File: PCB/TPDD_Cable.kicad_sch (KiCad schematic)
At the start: 9 parts, among them J1 TPDD_RS-232C, P3 RX, P4 RTS, P5 CTS, P6 DSR, Q1 DTA114EKA, Q2 DTA114EKA, Q3 DTA114EKA

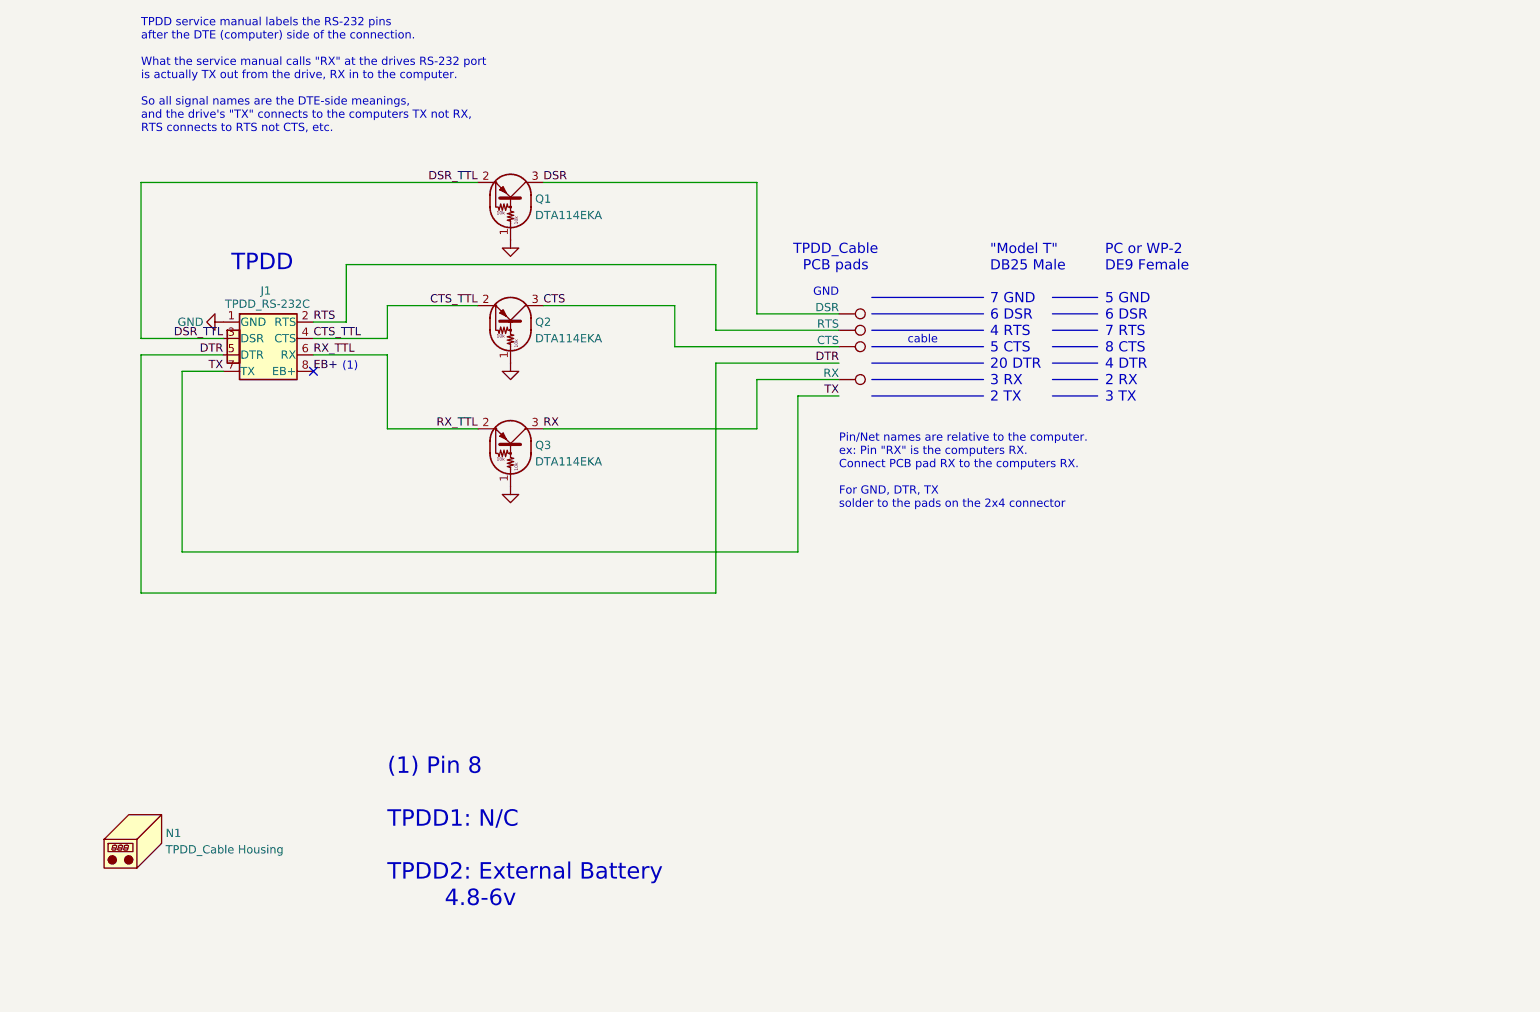
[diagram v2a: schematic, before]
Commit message: db25 pinout pics, enlarge ziptie holes to 3mm
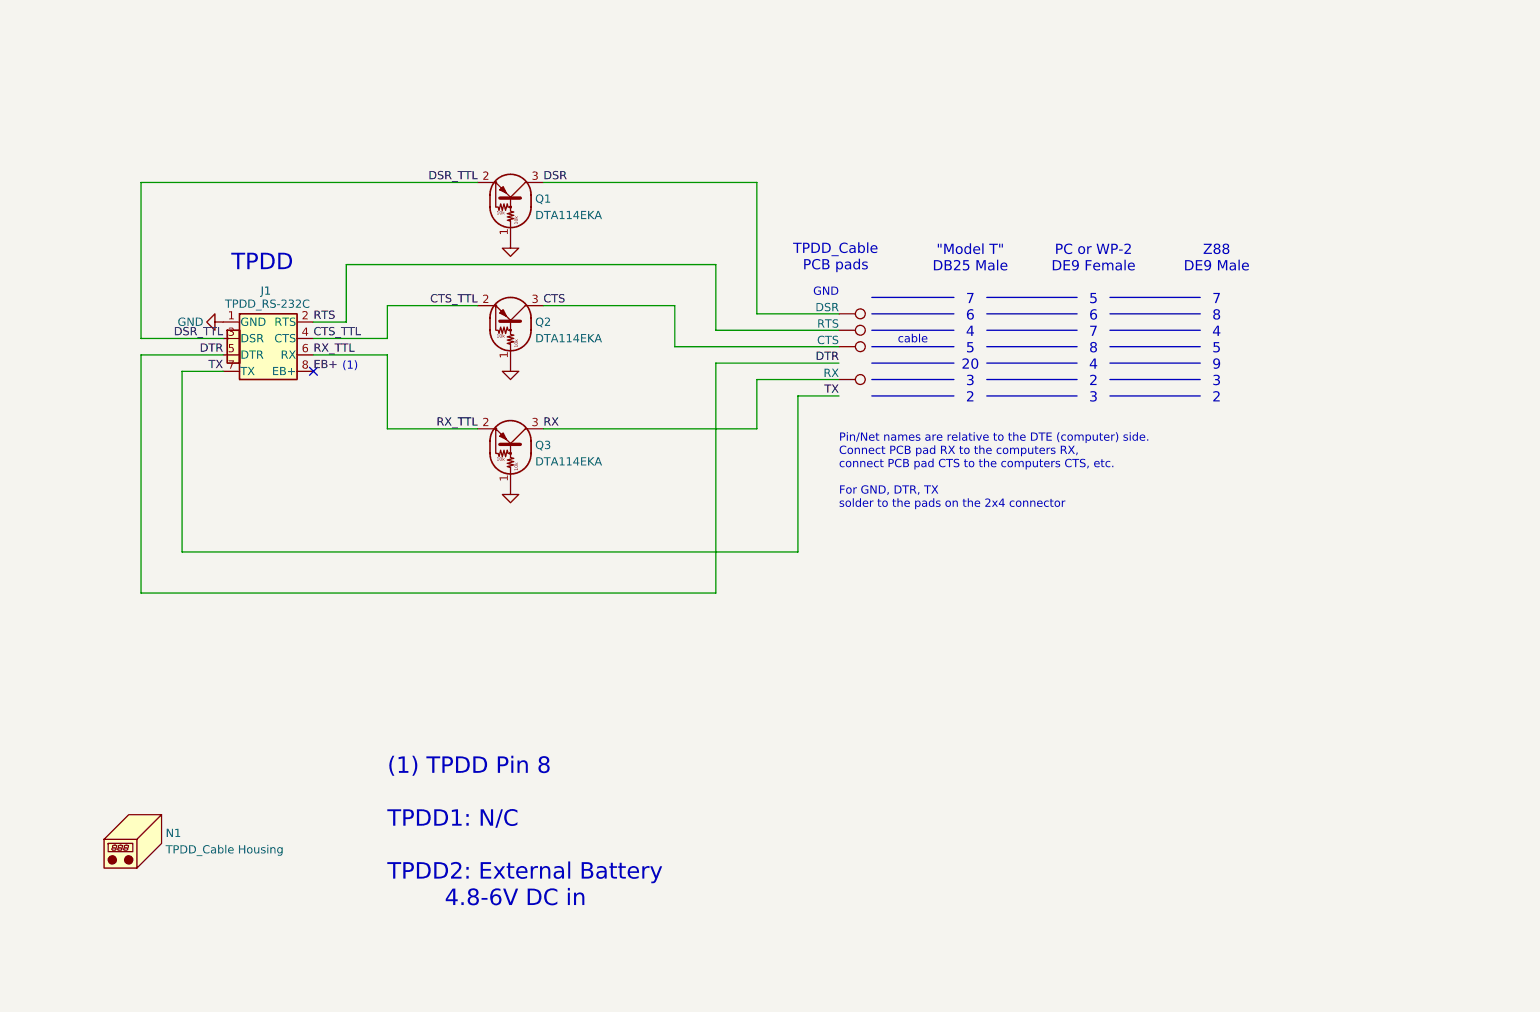
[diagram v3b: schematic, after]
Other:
- note added: ""Model T" DB25 Male 7 6 4 5 20 3 2"
- note added: "(1) TPDD Pin 8 TPDD1: N/C TPDD2: External Battery 4.8-6V DC in"
- note added: "PC or WP-2 DE9 Female 5 6 7 8 4 2 3"
- note added: "Pin/Net names are relative to the DTE (computer) side. Connect PCB pad RX to the computers RX, connect PCB pad CTS to the computers CTS, etc. For GND, DTR, TX solder to the pads on the 2x4 connector"
- note added: "Z88 DE9 Male 7 8 4 5 9 3 2"
- note removed: ""Model T" DB25 Male 7 GND 6 DSR 4 RTS 5 CTS 20 DTR 3 RX 2 TX"
- note removed: "(1) Pin 8 TPDD1: N/C TPDD2: External Battery 4.8-6v"
- note removed: "PC or WP-2 DE9 Female 5 GND 6 DSR 7 RTS 8 CTS 4 DTR 2 RX 3 TX"
- note removed: "Pin/Net names are relative to the computer. ex: Pin "RX" is the computers RX. Connect PCB pad RX to the computers RX. For GND, DTR, TX solder to the pads on the 2x4 connector"
- note removed: "TPDD service manual labels the RS-232 pins after the DTE (computer) side of the connection. What the service manual calls "RX" at the drives RS-232 port is actually TX out from the drive, RX in to the computer. So all signal names are the DTE-side meanings, and the drive's "TX" connects to the computers TX not RX, RTS connects to RTS not CTS, etc."
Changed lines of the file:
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@@
 		(title "TPDD-RS-232")
 		(date "2024-10-23")
-		(rev "5")
+		(rev "6")
 		(company "Brian K. White")
 	)
@@
 	(polyline
 		(pts
-			(xy 204.47 96.52) (xy 211.455 96.52)
+			(xy 194.31 96.52) (xy 208.28 96.52)
 		)
 		(stroke
@@
 	(polyline
 		(pts
-			(xy 204.47 86.36) (xy 211.455 86.36)
-		)
-		(stroke
-			(width 0)
-			(type default)
-		)
-	)
-	(polyline
-		(pts
-			(xy 176.53 86.36) (xy 193.802 86.36)
+			(xy 194.31 86.36) (xy 208.28 86.36)
+		)
+		(stroke
+			(width 0)
+			(type default)
+		)
+	)
+	(polyline
+		(pts
+			(xy 213.36 88.9) (xy 227.33 88.9)
+		)
+		(stroke
+			(width 0)
+			(type default)
+		)
+	)
+	(polyline
+		(pts
+			(xy 176.53 86.36) (xy 189.23 86.36)
+		)
+		(stroke
+			(width 0)
+			(type default)
+		)
+	)
+	(polyline
+		(pts
+			(xy 213.36 96.52) (xy 227.33 96.52)
 		)
 		(stroke
@@
 	(polyline
 		(pts
-			(xy 176.53 93.98) (xy 193.802 93.98)
+			(xy 176.53 93.98) (xy 189.23 93.98)
 		)
 		(stroke
@@
 	(polyline
 		(pts
-			(xy 204.47 81.28) (xy 211.455 81.28)
+			(xy 194.31 81.28) (xy 208.28 81.28)
 		)
 		(stroke
@@
 	(polyline
 		(pts
-			(xy 176.53 88.9) (xy 193.802 88.9)
+			(xy 176.53 88.9) (xy 189.23 88.9)
 		)
 		(stroke
@@
 		)
 	)
+	(polyline
+		(pts
+			(xy 213.36 86.36) (xy 227.33 86.36)
+		)
+		(stroke
+			(width 0)
+			(type default)
+		)
+	)
 	(wire
 		(pts
@@
 		)
 	)
+	(polyline
+		(pts
+			(xy 213.36 91.44) (xy 227.33 91.44)
+		)
+		(stroke
+			(width 0)
+			(type default)
+		)
+	)
 	(wire
 		(pts
@@
 	(polyline
 		(pts
-			(xy 204.47 88.9) (xy 211.455 88.9)
-		)
-		(stroke
-			(width 0)
-			(type default)
-		)
-	)
-	(polyline
-		(pts
-			(xy 176.53 81.28) (xy 193.802 81.28)
+			(xy 194.31 88.9) (xy 208.28 88.9)
+		)
+		(stroke
+			(width 0)
+			(type default)
+		)
+	)
+	(polyline
+		(pts
+			(xy 213.36 83.82) (xy 227.33 83.82)
+		)
+		(stroke
+			(width 0)
+			(type default)
+		)
+	)
+	(polyline
+		(pts
+			(xy 176.53 81.28) (xy 189.23 81.28)
 		)
 		(stroke
@@
 	(polyline
 		(pts
-			(xy 204.47 93.98) (xy 211.455 93.98)
-		)
-		(stroke
-			(width 0)
-			(type default)
-		)
-	)
-	(polyline
-		(pts
-			(xy 176.53 91.44) (xy 193.802 91.44)
-		)
-		(stroke
-			(width 0)
-			(type default)
-		)
-	)
-	(polyline
-		(pts
-			(xy 176.53 96.52) (xy 193.802 96.52)
+			(xy 194.31 93.98) (xy 208.28 93.98)
+		)
+		(stroke
+			(width 0)
+			(type default)
+		)
+	)
+	(polyline
+		(pts
+			(xy 176.53 91.44) (xy 189.23 91.44)
+		)
+		(stroke
+			(width 0)
+			(type default)
+		)
+	)
+	(polyline
+		(pts
+			(xy 176.53 96.52) (xy 189.23 96.52)
 		)
 		(stroke
@@
 	(polyline
 		(pts
-			(xy 204.47 91.44) (xy 211.455 91.44)
-		)
-		(stroke
-			(width 0)
-			(type default)
-		)
-	)
-	(polyline
-		(pts
-			(xy 176.53 83.82) (xy 193.802 83.82)
+			(xy 194.31 91.44) (xy 208.28 91.44)
+		)
+		(stroke
+			(width 0)
+			(type default)
+		)
+	)
+	(polyline
+		(pts
+			(xy 176.53 83.82) (xy 189.23 83.82)
+		)
+		(stroke
+			(width 0)
+			(type default)
+		)
+	)
+	(polyline
+		(pts
+			(xy 213.36 81.28) (xy 227.33 81.28)
+		)
+		(stroke
+			(width 0)
+			(type default)
+		)
+	)
+	(polyline
+		(pts
+			(xy 213.36 93.98) (xy 227.33 93.98)
 		)
 		(stroke
@@
 	(polyline
 		(pts
-			(xy 204.47 83.82) (xy 211.455 83.82)
+			(xy 194.31 83.82) (xy 208.28 83.82)
 		)
 		(stroke
@@
 		)
 	)
+	(text "Z88\nDE9 Male\n\n7\n8\n4\n5\n9\n3\n2"
+		(exclude_from_sim no)
+		(at 229.87 73.152 0)
+		(effects
+			(font
+				(size 1.5748 1.5748)
+			)
+			(justify top)
+		)
+	)
 	(text "TPDD_Cable\nPCB pads"
 		(exclude_from_sim no)
@@
 		)
 	)
-	(text "(1) Pin 8\n\nTPDD1: N/C\n\nTPDD2: External Battery\n        4.8-6v"
+	(text "(1) TPDD Pin 8\n\nTPDD1: N/C\n\nTPDD2: External Battery\n        4.8-6V DC in"
 		(exclude_from_sim no)
 		(at 101.6 152.4 0)
@@
 	(text "cable"
 		(exclude_from_sim no)
-		(at 184.404 87.884 0)
+		(at 182.88 87.884 0)
 		(effects
 			(font
@@
 		)
 	)
-	(text "TPDD service manual labels the RS-232 pins\nafter the DTE (computer) side of the connection.\n\nWhat the service manual calls \"RX\" at the drives RS-232 port\nis actually TX out from the drive, RX in to the computer.\n\nSo all signal names are the DTE-side meanings,\nand the drive's \"TX\" connects to the computers TX not RX,\nRTS connects to RTS not CTS, etc.\n"
-		(exclude_from_sim no)
-		(at 63.5 38.1 0)
+	(text "Pin/Net names are relative to the DTE (computer) side.\nConnect PCB pad RX to the computers RX,\nconnect PCB pad CTS to the computers CTS, etc.\n\nFor GND, DTR, TX\nsolder to the pads on the 2x4 connector\n"
+		(exclude_from_sim no)
+		(at 171.45 102.362 0)
 		(effects
 			(font
@@
 		)
 	)
-	(text "Pin/Net names are relative to the computer.\nex: Pin \"RX\" is the computers RX.\nConnect PCB pad RX to the computers RX.\n\nFor GND, DTR, TX\nsolder to the pads on the 2x4 connector\n"
-		(exclude_from_sim no)
-		(at 171.45 102.362 0)
-		(effects
-			(font
-				(size 1.27 1.27)
-			)
-			(justify left top)
-		)
-	)
-	(text "PC or WP-2\nDE9 Female\n\n5 GND\n6 DSR\n7 RTS\n8 CTS\n4 DTR\n2 RX\n3 TX"
-		(exclude_from_sim no)
-		(at 212.598 85.344 0)
+	(text "PC or WP-2\nDE9 Female\n\n5\n6\n7\n8\n4\n2\n3"
+		(exclude_from_sim no)
+		(at 210.82 73.152 0)
 		(effects
 			(font
 				(size 1.5748 1.5748)
 			)
-			(justify left)
+			(justify top)
 		)
 	)
@@
 		)
 	)
-	(text "\"Model T\"\nDB25 Male\n\n7 GND\n6 DSR\n4 RTS\n5 CTS\n20 DTR\n3 RX\n2 TX"
-		(exclude_from_sim no)
-		(at 194.818 85.344 0)
+	(text "\"Model T\"\nDB25 Male\n\n7\n6\n4\n5\n20\n3\n2"
+		(exclude_from_sim no)
+		(at 191.77 73.152 0)
 		(effects
 			(font
 				(size 1.5748 1.5748)
 			)
-			(justify left)
-		)
-	)
+			(justify top)
+		)
+	)

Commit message: schematics notes text
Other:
- note removed: "GND"
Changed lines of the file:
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@@
+		)
+	)
+	(wire
+		(pts
+			(xy 167.64 81.28) (xy 171.45 81.28)
+		)
+		(stroke
+			(width 0)
+			(type default)
 		)
 	)
@@
 			)
 			(justify left top)
-		)
-	)
-	(text "GND"
-		(exclude_from_sim no)
-		(at 171.45 81.28 0)
-		(effects
-			(font
-				(size 1.27 1.27)
-			)
-			(justify right bottom)
 		)
 	)
@@
 	(label "CTS_TTL"
 		(at 115.57 82.55 180)
+		(fields_autoplaced yes)
+		(effects
+			(font
+				(size 1.27 1.27)
+			)
+			(justify right bottom)
+		)
+	)
+	(label "GND"
+		(at 171.45 81.28 180)
 		(fields_autoplaced yes)
 		(effects
@@
 					(unit 1)
 				)
+			)
+		)
+	)
+	(symbol
+		(lib_id "000_LOCAL:GND")
+		(at 167.64 81.28 270)
+		(unit 1)
+		(exclude_from_sim no)
+		(in_bom yes)
+		(on_board yes)
+		(dnp no)
+		(property "Reference" "#PWR01"
+			(at 161.29 81.28 0)
+			(effects
+				(font
+					(size 1.27 1.27)
+				)
+				(hide yes)
+			)
+		)
+		(property "Value" "GND"
+			(at 164.592 81.28 90)
+			(effects
+				(font
+					(size 1.27 1.27)
+				)
+				(justify right)
+			)
+		)
+		(property "Footprint" ""
+			(at 167.64 81.28 0)
+			(effects
+				(font
+					(size 1.27 1.27)
+				)
+				(hide yes)
+			)
+		)
+		(property "Datasheet" ""
+			(at 167.64 81.28 0)
+			(effects
+				(font
+					(size 1.27 1.27)
+				)
+				(hide yes)
+			)
+		)
+		(property "Description" ""
+			(at 167.64 81.28 0)
+			(effects
+				(font
+					(size 1.27 1.27)
+				)
+				(hide yes)
+			)
+		)
+		(pin "1"
+		)
+		(instances
+			(project "TPDD_Cable"
+				(path "/0d433bab-64ac-46dd-8906-cd1b476f2235"
+					(reference "#PWR01")
+					(unit 1)
+				)
